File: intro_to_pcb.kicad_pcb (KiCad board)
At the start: 2 copper layers, 81.5 x 47.5 mm, 45 parts, among them J1 USB_C_Receptacle_USB2.0_16P, J2 Conn_01x16_Socket, J3 Conn_01x16_Socket, J4 ISCP, SW1 SW_Push, U1 ATmega328P-A, U2 LM1117MP-ADJ, U3 FT232RL, Y1 16MHz

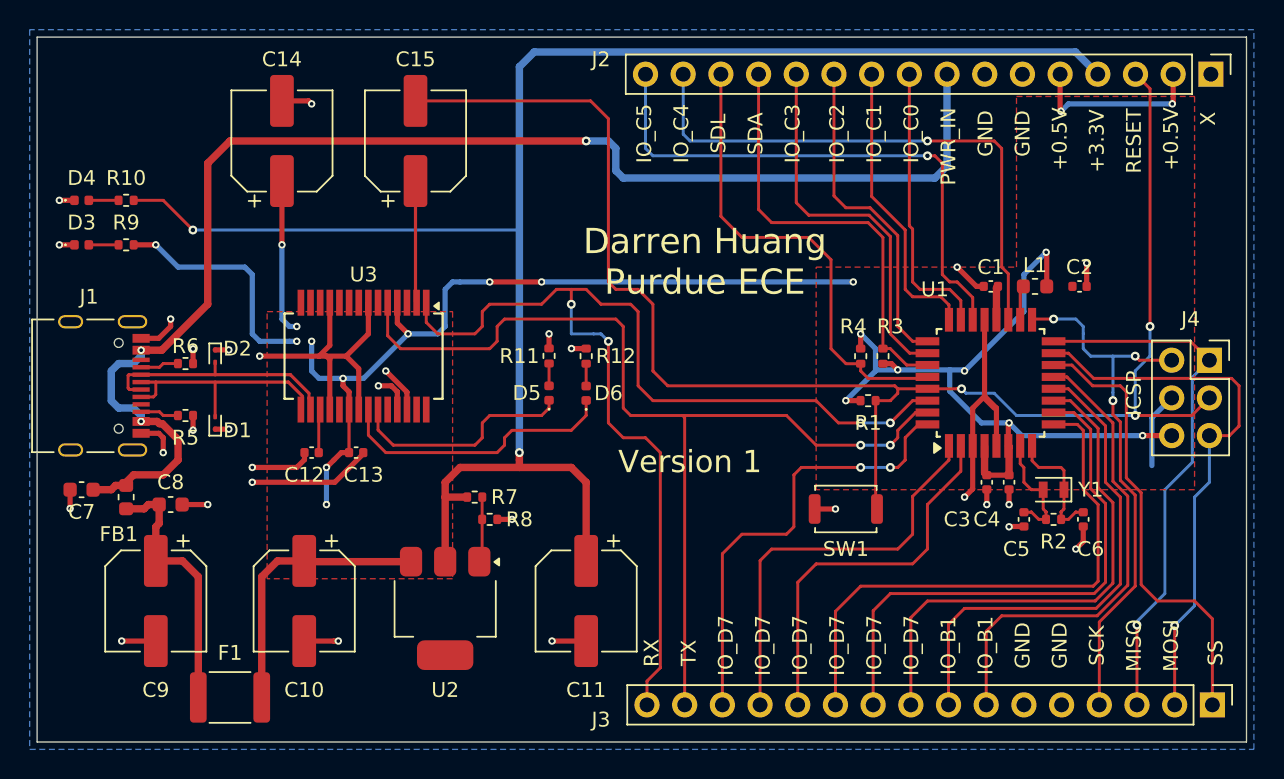
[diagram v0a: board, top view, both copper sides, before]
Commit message: delete zones for footprint editing
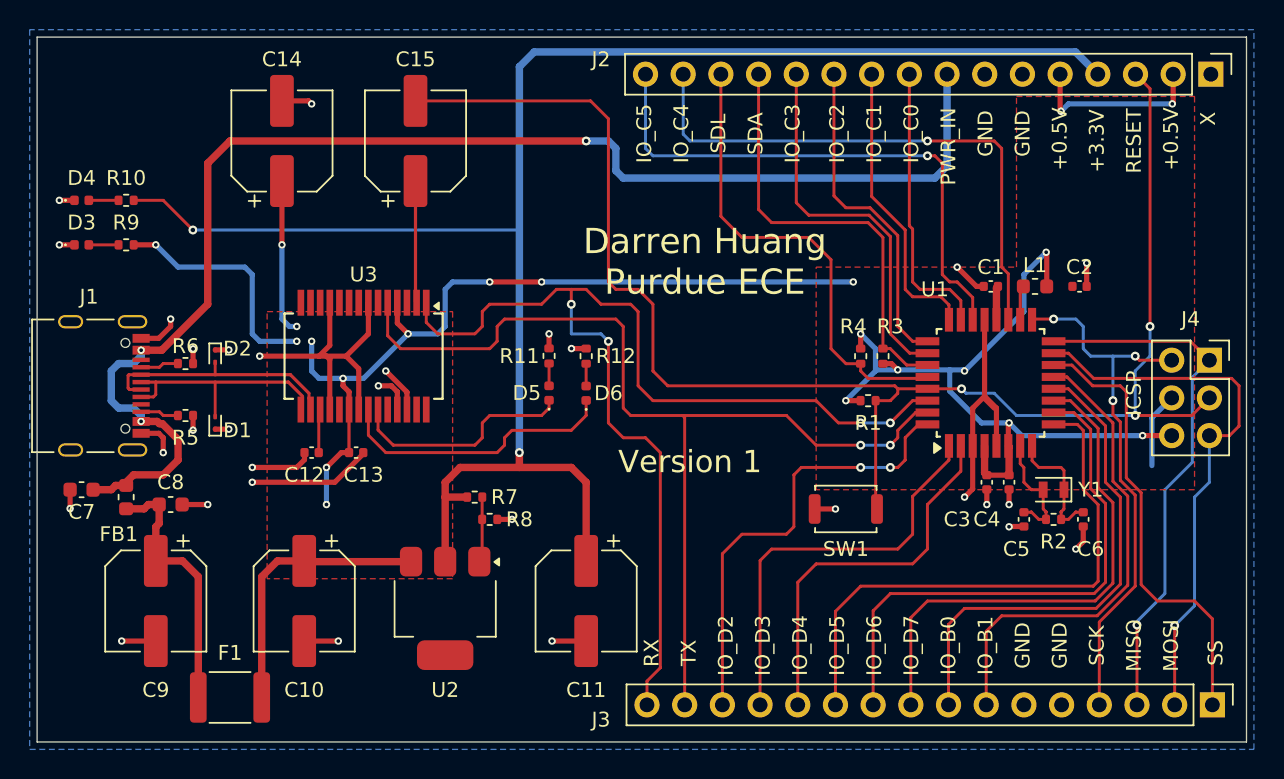
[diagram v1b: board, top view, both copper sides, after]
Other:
- board text added: "IO_B0"
- board text added: "IO_D2"
- board text added: "IO_D3"
- board text added: "IO_D4"
- board text added: "IO_D5"
- board text added: "IO_D6"

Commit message: .lck gitignore
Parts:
- C1, C2: footprint Capacitor_SMD:C_0402_1005Metric -> Capacitor_SMD:C_0603_1608Metric
- U2: footprint Package_TO_SOT_SMD:SOT-223 -> Package_TO_SOT_SMD:SOT-223-3_TabPin2
- moved C1 0.83 mm to (165.5, 116.0)
- moved C2 0.81 mm to (173.0, 116.0)
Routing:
- net +5V: track 164.6 -> 96.4 mm, vias 21 -> 10
- net GND: track 98.7 -> 34.2 mm, vias 30 -> 0
- net GPIO_C1: track 19.8 -> 19.2 mm
- removed copper zone on F.Cu, net +5V
- removed copper zone on B.Cu, net GND
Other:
- board text added: "Version 2"
- board text removed: "Version 1"

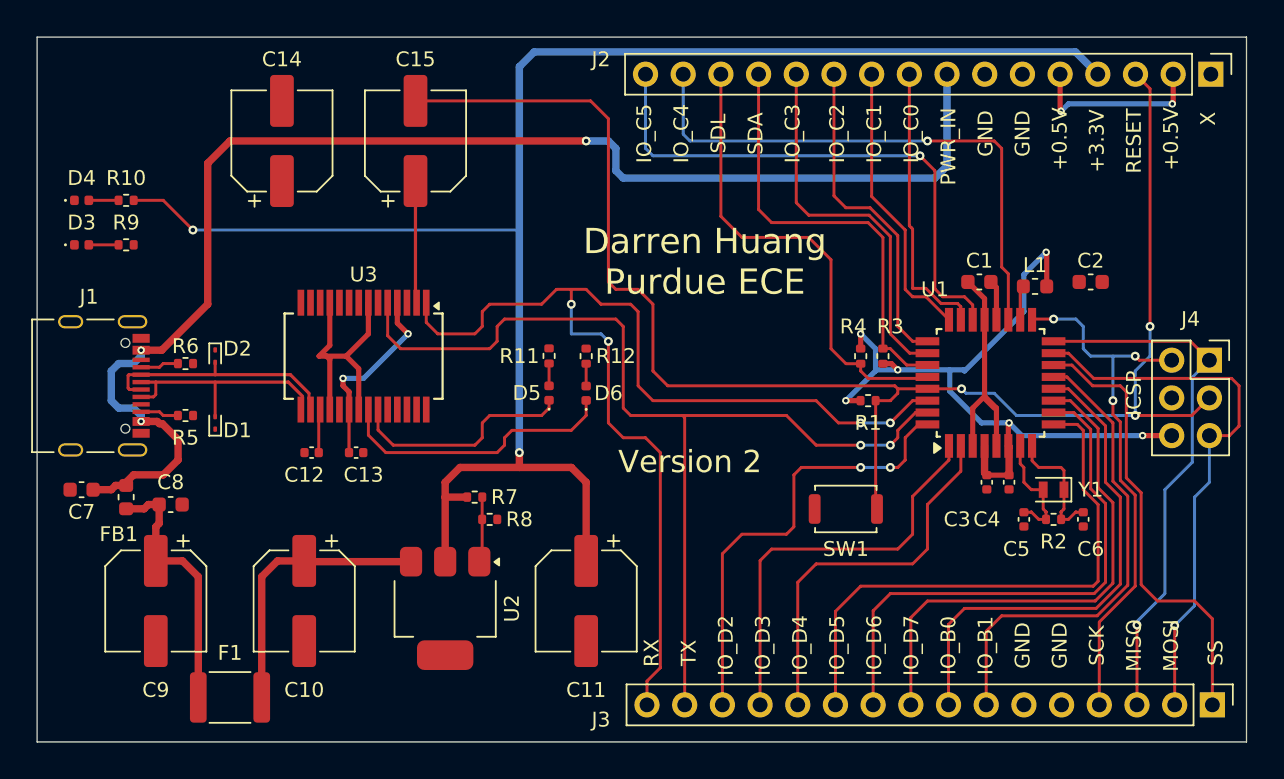
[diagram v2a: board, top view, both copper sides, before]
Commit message: routed new 0603 footprints
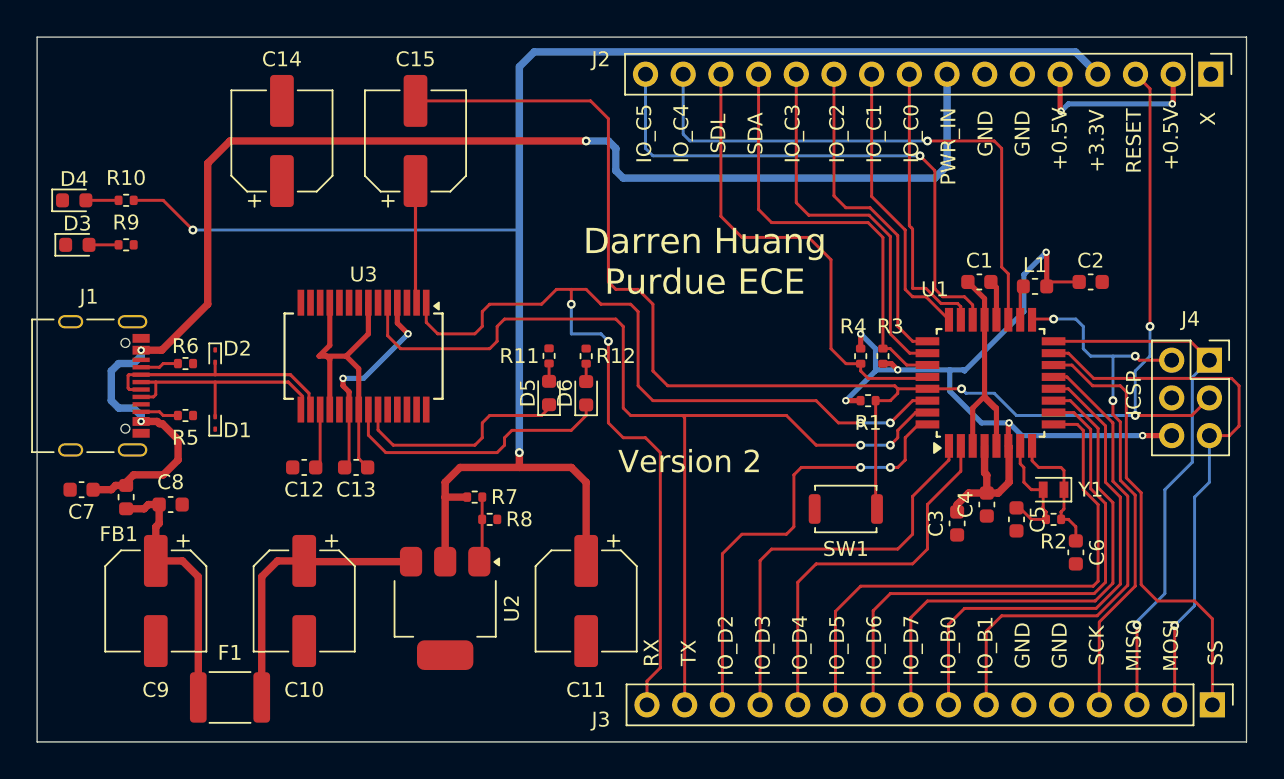
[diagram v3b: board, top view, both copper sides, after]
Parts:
- C12, C13, C3, C4, C5, C6: footprint Capacitor_SMD:C_0402_1005Metric -> Capacitor_SMD:C_0603_1608Metric
- D3, D4, D5, D6: footprint LED_SMD:LED_0402_1005Metric -> LED_SMD:LED_0603_1608Metric
- moved C3 3.42 mm to (164.0, 132.3)
- moved C6 2.28 mm to (172.0, 134.2)
- moved C4 2.12 mm to (166.0, 131.0)
- moved C12 1.12 mm to (120.0, 128.5)
- moved C13 1.00 mm to (123.5, 128.5)
- moved C5 0.50 mm to (168.0, 132.0)
- moved D4 0.50 mm to (104.5, 110.5)
- moved D3 0.29 mm to (104.7, 113.5)
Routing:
- net +5V: track 96.4 -> 104.6 mm
- net GND: track 34.2 -> 38.3 mm
- net Net-(U3-3V3OUT): track 2.94 -> 4.16 mm
- net OSC_1: track 7.85 -> 8.76 mm

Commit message: routed 0603 footprints
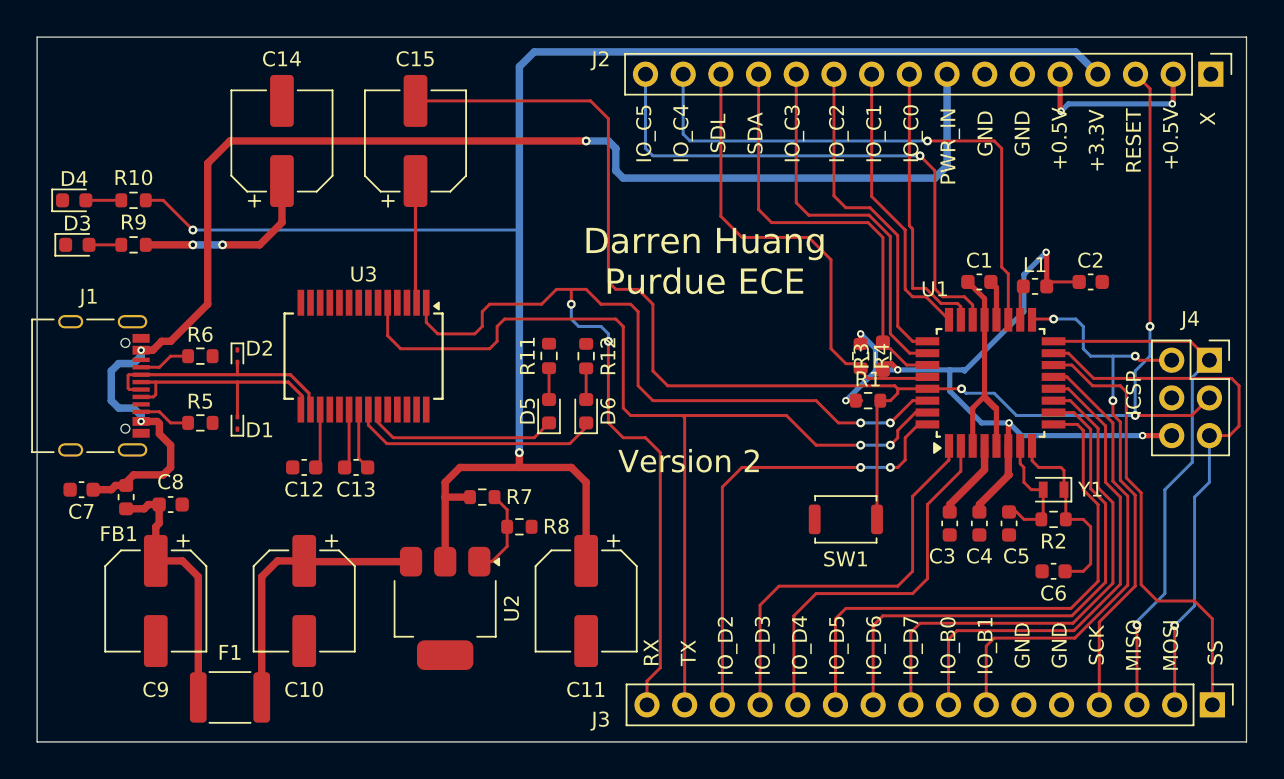
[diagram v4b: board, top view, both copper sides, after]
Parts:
- R1, R10, R11, R12, R2, R4, R5, R6, R7, R8, R9: footprint Resistor_SMD:R_0402_1005Metric -> Resistor_SMD:R_0603_1608Metric
- R3: footprint Resistor_SMD:R_0402_1005Metric -> Resistor_SMD:R_0603_1608Metric_Pad0.98x0.95mm_HandSolder
- moved R8 2.06 mm to (134.5, 132.5)
- moved C6 1.97 mm to (170.5, 135.5), turned to 180 degrees
- moved D1 1.50 mm to (115.5, 125.5)
- moved D2 1.50 mm to (115.5, 121.0)
- moved C4 1.37 mm to (165.5, 132.3)
- moved D5 1.23 mm to (136.5, 124.7)
- moved D6 1.21 mm to (139.0, 124.7)
- moved R5 1.12 mm to (113.0, 125.5)
- moved R6 1.12 mm to (113.0, 121.0)
- moved SW1 0.70 mm to (156.5, 132.0)
- moved C5 0.57 mm to (167.5, 132.3)
- moved R7 0.51 mm to (132.0, 130.5)
- moved C3 0.50 mm to (163.5, 132.3)
- moved R10 0.50 mm to (108.5, 110.5)
- moved R9 0.50 mm to (108.5, 113.5)
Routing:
- net GND: track 38.3 -> 20.7 mm
- net OSC_2: track 8.95 -> 13.2 mm
- net +5V: track 104.6 -> 107.3 mm
- net Net-(D5-K): track 15.5 -> 13.2 mm
- net Net-(D6-K): track 19.2 -> 17.0 mm
- net Net-(U2-ADJ): track 4.43 -> 5.98 mm
- net Net-(J1-CC2): track 2.58 -> 3.48 mm
- net Net-(J1-CC1): track 2.58 -> 3.48 mm
- net RESET: track 105.0 -> 105.8 mm
- net +3.3V: track 116.3 -> 115.7 mm
- net Net-(D5-A): track 1.50 -> 2.11 mm
- net Net-(D6-A): track 1.50 -> 2.10 mm
- net GPIO_B0: track 33.7 -> 33.2 mm
- net GPIO_D2: track 30.5 -> 31.1 mm
- net GPIO_B1: track 32.4 -> 31.8 mm
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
